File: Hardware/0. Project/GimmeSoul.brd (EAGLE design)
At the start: 68.6 x 53.5 mm, 24 parts, among them CN1 2.1MMJACKTHM, U1 ATMEGA328P-AU, U2 REG1117-5.0

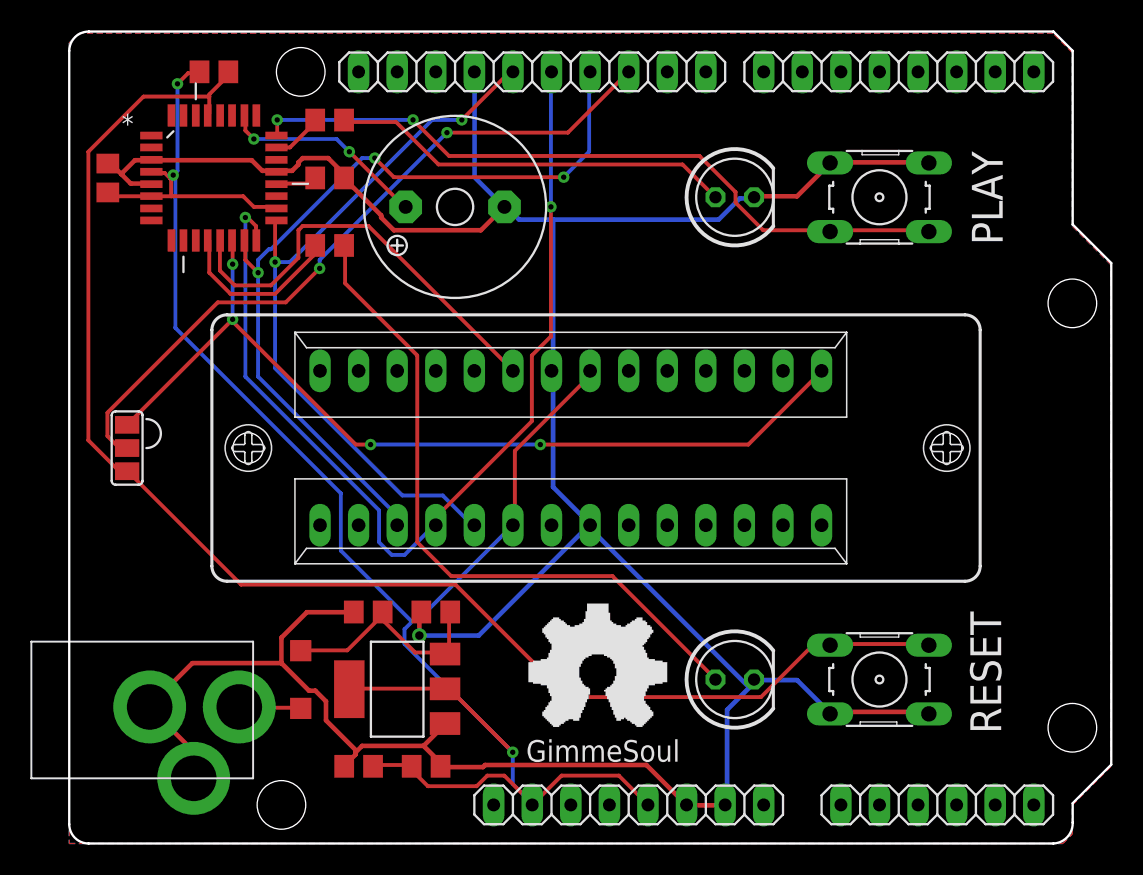
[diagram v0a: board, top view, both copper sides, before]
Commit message: Jumpers on PCB layout bug fix
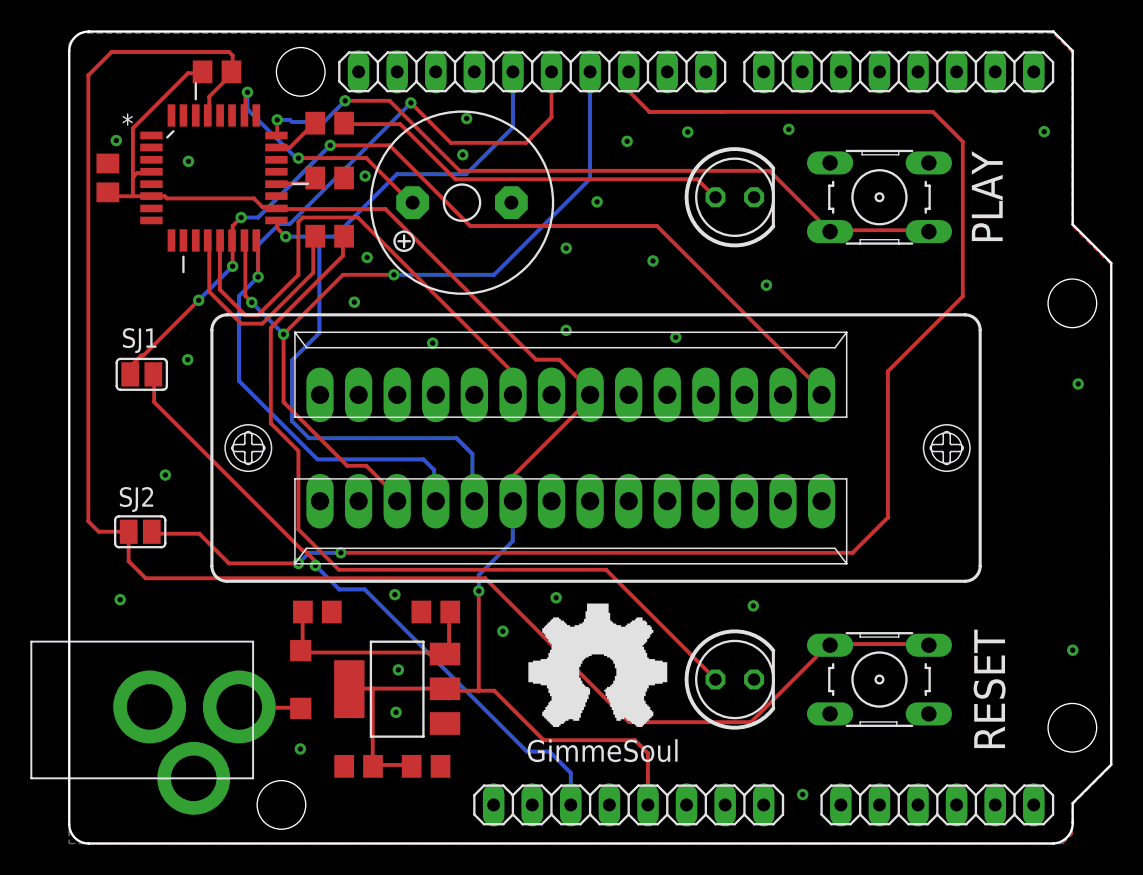
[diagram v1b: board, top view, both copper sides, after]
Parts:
- added SJ2: (no value), jumper:SJ
- SJ1: device jumper:SJ_2 -> jumper:SJ
- moved SJ1 4.95 mm to (4.78, 30.9), turned to 0 degrees
- moved C3 3.35 mm to (16.3, 15.2), turned to 0 degrees
- moved R3 0.61 mm to (17.1, 40.0)
- moved SG5 0.54 mm to (25.9, 42.2)
- moved R2 0.20 mm to (17.1, 47.4)
- moved R1 0.20 mm to (9.73, 50.8)
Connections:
- new net N$6: JP1.3, SJ1.2
- net +5V: no longer JP1.2
- net ICSP_RESET: now also SJ2.1; no longer SJ1.3
- net N$5: now also SJ2.2; no longer SJ1.2
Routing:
- net GND: track 207.5 -> 0.00 mm, vias 1 -> 31
- net N$5: track 47.1 -> 102.1 mm
- net N$6: track 0.00 -> 41.7 mm, vias 0 -> 1
- net +5V: track 129.9 -> 104.5 mm, vias 3 -> 1
- net ICSP_RESET: track 95.8 -> 108.4 mm
- net N$3: track 44.9 -> 53.6 mm
- net ICSP_MISO: track 64.8 -> 57.3 mm
- net 8MHZ_CLOCK: track 28.3 -> 33.6 mm
- net ICSP_CLK: track 48.1 -> 51.7 mm, vias 2 -> 1
- net LED_ERROR: track 11.4 -> 15.1 mm
- net BUZZER: track 13.7 -> 16.1 mm
- net !ICSP_SS: track 59.3 -> 60.6 mm
- net ICSP_MOSI: track 54.9 -> 54.1 mm
- net BUTTON_RUN: track 47.5 -> 48.3 mm

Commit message: 16MHz crystal added to MCU
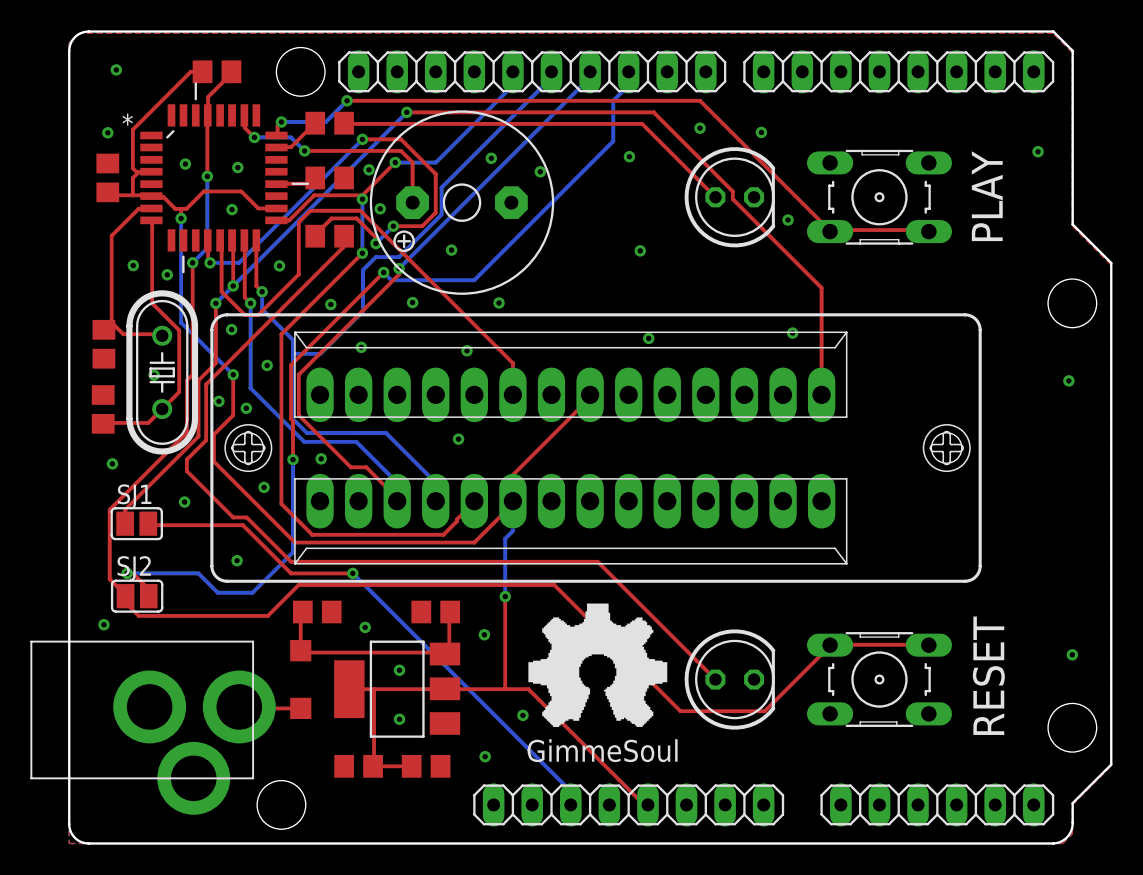
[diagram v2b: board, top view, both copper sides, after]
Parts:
- added C7, C8: 22pF, rcl:C0805
- added Q1: 16 MHz, crystal:HC49/S
- moved SJ1 9.84 mm to (4.45, 21.1)
- moved SJ2 4.25 mm to (4.47, 16.3)
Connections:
- new net N$7: C7.2, Q1.1, U1.7
- new net N$8: C8.2, Q1.2, U1.8
- net GND: now also C7.1, C8.1
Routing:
- net N$5: track 102.1 -> 60.0 mm, vias 2 -> 3
- net LED_ERROR: track 15.1 -> 33.5 mm, vias 0 -> 4
- net N$8: track 0.00 -> 18.0 mm
- net !ICSP_SS: track 60.6 -> 77.2 mm, vias 4 -> 3
- net N$7: track 0.00 -> 14.2 mm
- net +5V: track 104.5 -> 118.1 mm, vias 1 -> 3
- net ICSP_RESET: track 108.4 -> 98.2 mm, vias 0 -> 2
- net ICSP_MOSI: track 54.1 -> 62.8 mm, vias 3 -> 2
- net N$3: track 53.6 -> 60.2 mm
- net N$6: track 41.7 -> 36.1 mm
- net ICSP_CLK: track 51.7 -> 57.2 mm, vias 1 -> 3
- net ICSP_MISO: track 57.3 -> 52.7 mm, vias 2 -> 1
- net 8MHZ_CLOCK: track 33.6 -> 34.3 mm
- net BUZZER: track 16.1 -> 15.5 mm

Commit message: PCB layout minor improvements
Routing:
- net N$5: track 60.0 -> 55.9 mm
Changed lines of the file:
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@@
 <drawing>
 <settings>
-<setting alwaysvectorfont="yes"/>
+<setting alwaysvectorfont="no"/>
 <setting verticaltext="up"/>
 </settings>
@@
 <contactref element="JP2" pad="3"/>
 <contactref element="SJ2" pad="2"/>
-<wire x1="5.207" y1="16.764" x2="5.207" y2="16.383" width="0.254" layer="1"/>
-<wire x1="4.191" y1="17.78" x2="5.207" y2="16.764" width="0.254" layer="1"/>
-<wire x1="3.81" y1="17.78" x2="4.191" y2="17.78" width="0.254" layer="1"/>
+<wire x1="6.7818" y1="16.4338" x2="5.207" y2="16.4338" width="0.254" layer="1"/>
+<wire x1="5.207" y1="16.4338" x2="5.207" y2="16.383" width="0.254" layer="1"/>
 <wire x1="14.732" y1="27.813" x2="14.732" y2="25.273" width="0.254" layer="1"/>
 <wire x1="14.605" y1="27.94" x2="14.732" y2="27.813" width="0.254" layer="1"/>
@@
 <wire x1="36.83" y1="50.8" x2="36.83" y2="49.911" width="0.254" layer="16"/>
 <wire x1="5.207" y1="16.383" x2="5.2324" y2="16.2814" width="0.254" layer="1"/>
-<via x="3.81" y="17.78" extent="1-16" drill="0.35"/>
+<via x="6.7818" y="16.4338" extent="1-16" drill="0.35"/>
 <via x="14.732" y="25.273" extent="1-16" drill="0.35"/>
 <via x="20.701" y="37.592" extent="1-16" drill="0.35"/>
-<wire x1="3.81" y1="17.78" x2="8.509" y2="17.78" width="0.254" layer="16"/>
-<wire x1="8.509" y1="17.78" x2="9.779" y2="16.51" width="0.254" layer="16"/>
-<wire x1="9.779" y1="16.51" x2="12.065" y2="16.51" width="0.254" layer="16"/>
+<wire x1="11.9634" y1="16.4084" x2="6.8072" y2="16.4084" width="0.254" layer="16"/>
+<wire x1="6.7818" y1="16.4338" x2="6.8072" y2="16.4084" width="0.254" layer="16"/>
 <wire x1="14.732" y1="19.177" x2="14.732" y2="25.273" width="0.254" layer="16"/>
-<wire x1="12.065" y1="16.51" x2="14.732" y2="19.177" width="0.254" layer="16"/>
+<wire x1="11.9634" y1="16.4084" x2="14.732" y2="19.177" width="0.254" layer="16"/>
 </signal>
 <signal name="N$6">

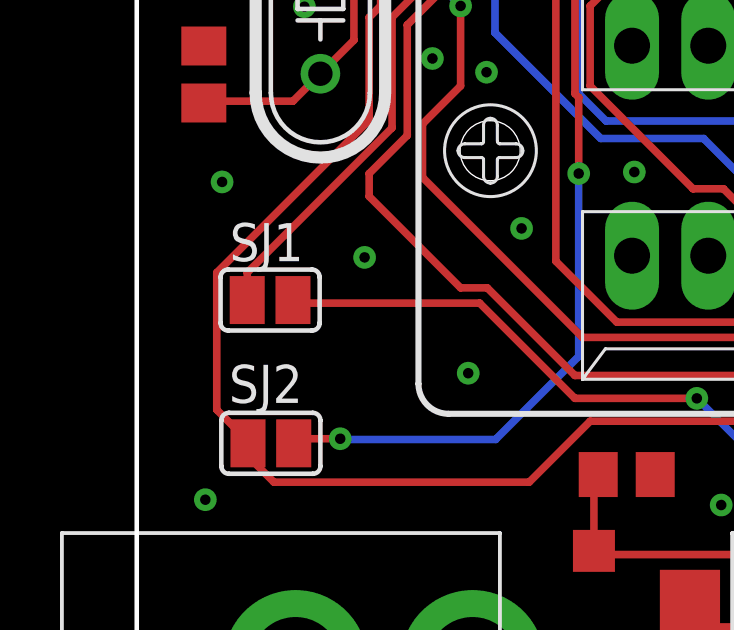
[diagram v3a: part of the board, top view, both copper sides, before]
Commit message: Silk Screen ref generated
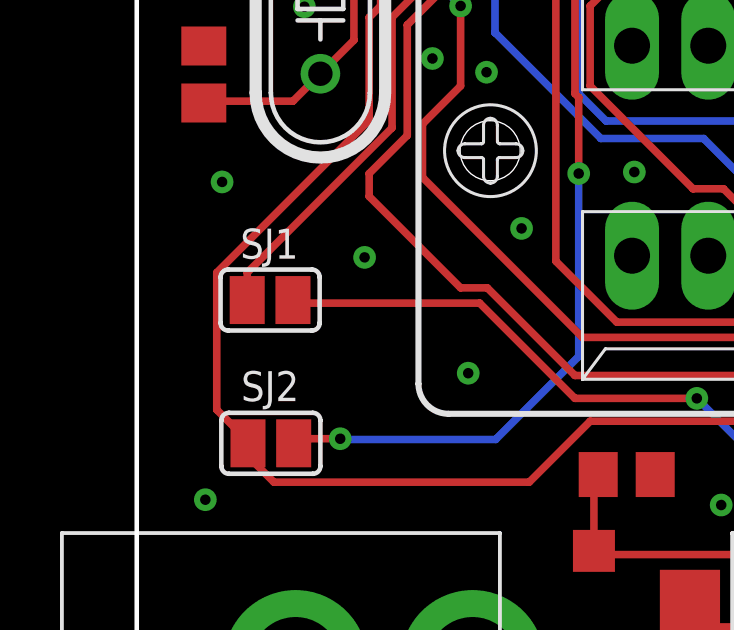
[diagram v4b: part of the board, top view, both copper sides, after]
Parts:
- C1, C2, C4, C6: value 100nF -> 100 nF / 50V
- C3, C5: value 1uF -> 1 uF / 50V
- C7, C8: value 22pF -> 22 pF / 50V
- CN1: value 2.1MMJACKTHM -> (none)
- R1: value 10k -> 10k ±5%
- R2, R3: value 100R -> 100R ±5%
- SG5: value 5V PASSIVE -> 5V Passive
- U1: value ATMEGA328P-AU -> (none)
- U2: value REG1117-5.0 -> LM1117MP-5.0
- ZX1: value 228-4817-00-0602J -> (none)
